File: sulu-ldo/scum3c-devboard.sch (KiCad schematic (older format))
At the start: 34 parts, among them J1 Conn_02x11_Odd_Even, J2 Conn_02x10_Odd_Even, J3 Conn_02x05_Odd_Even, J4 Conn_01x01_Male, U2 LP5907MFX-1.8, U3 TLV70311DBVR, U9AB1 ICM-20948

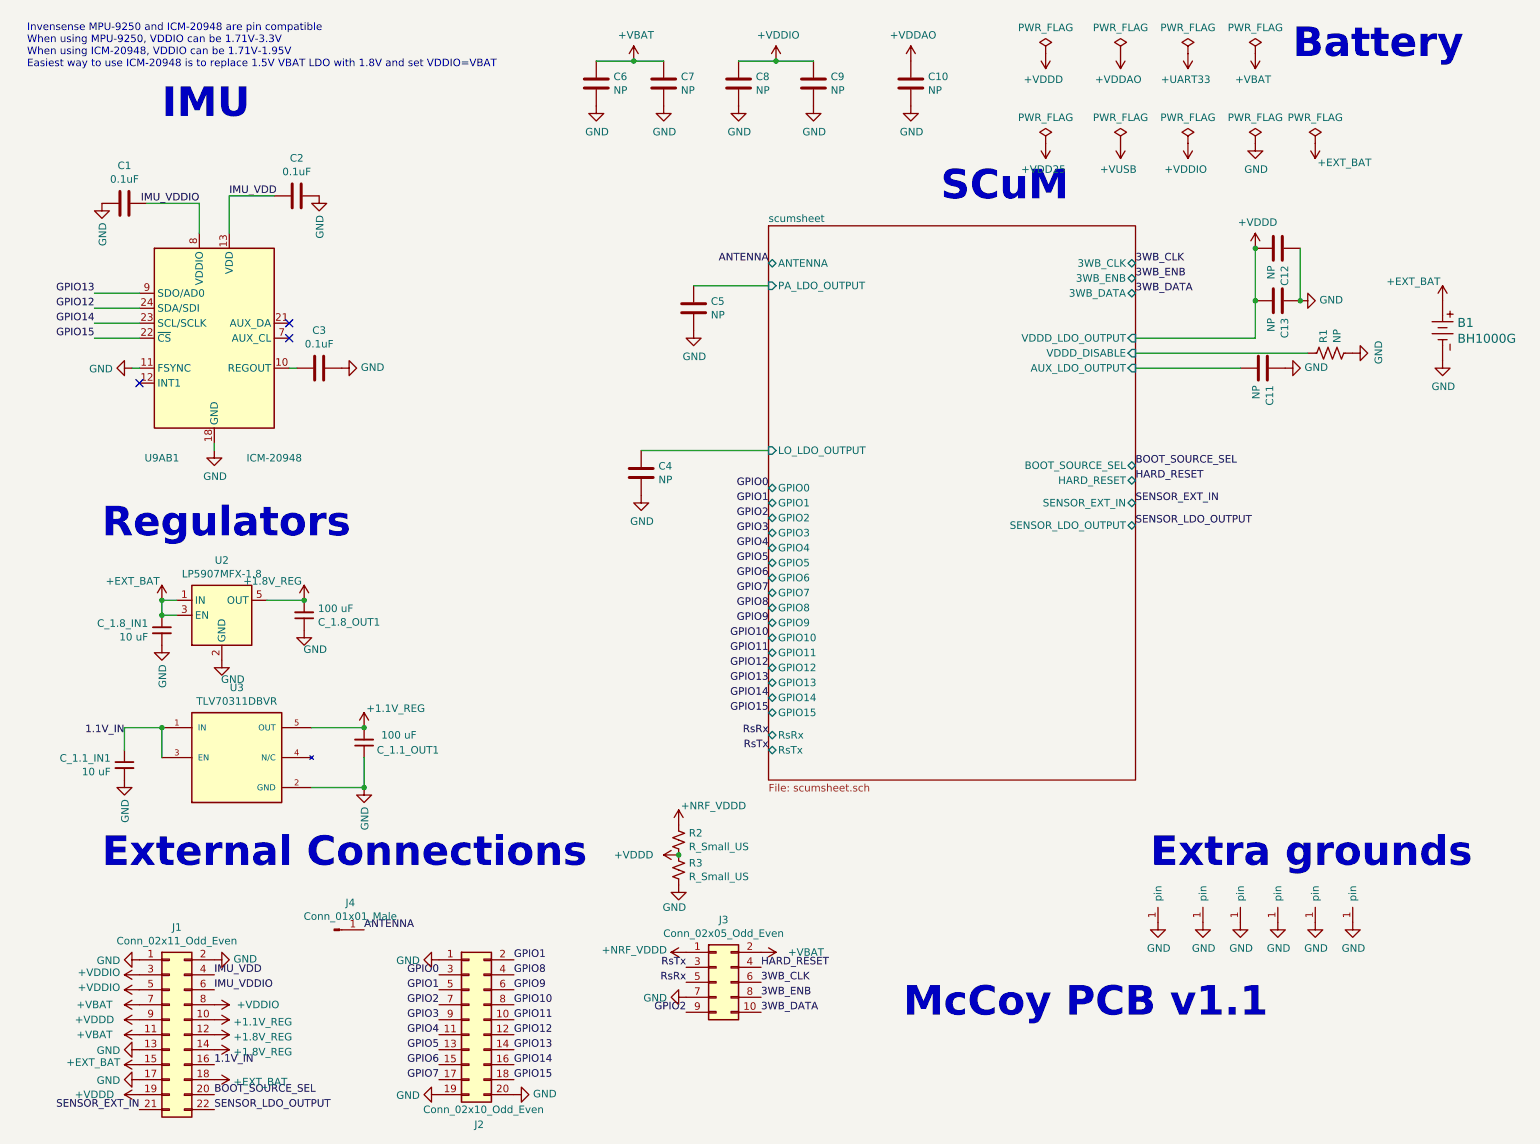
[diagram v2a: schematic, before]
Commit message: added ldos
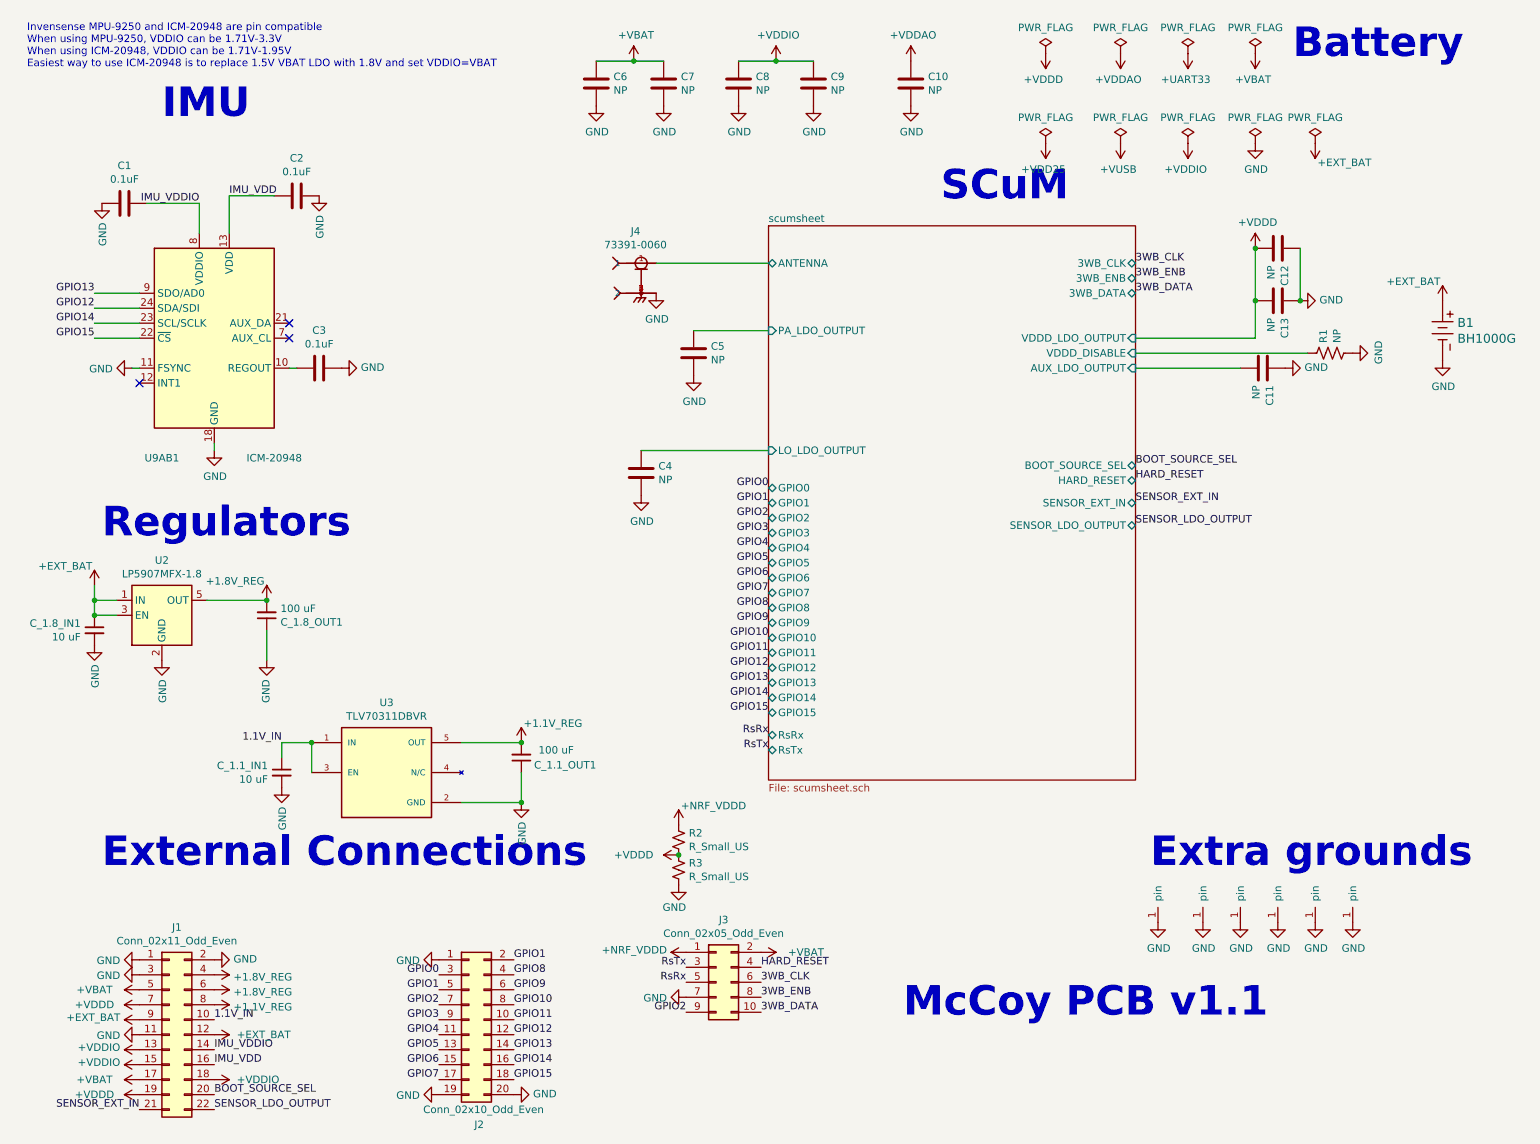
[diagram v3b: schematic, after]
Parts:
- removed J4: Conn_01x01_Male, Connector_PinHeader_2.54mm:PinHeader_1x01_P2.54mm_Vertical, symbol Connector:Conn_01x01_Male
- added J4: 73391-0060, downloaded_libs:MOLEX_73391-0060, symbol 73391-0060:73391-0060
- U3: footprint downloaded_libs:SOT95P280X145-5N -> SOT95P280X145-5N
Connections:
- net +1.1V_REG: now also J1.8 (Pin_8); no longer J1.10 (Pin_10)
- net +1.8V_REG: now also J1.4 (Pin_4), J1.6 (Pin_6); no longer J1.12 (Pin_12), J1.14 (Pin_14)
- net +EXT_BAT: now also J1.12 (Pin_12), J1.9 (Pin_9); no longer J1.15 (Pin_15), J1.18 (Pin_18)
- net +VBAT: now also J1.17 (Pin_17), J1.5 (Pin_5); no longer J1.11 (Pin_11), J1.7 (Pin_7)
- net +VDDD: now also J1.7 (Pin_7); no longer J1.9 (Pin_9)
- net +VDDIO: now also J1.13 (Pin_13), J1.15 (Pin_15), J1.18 (Pin_18); no longer J1.3 (Pin_3), J1.5 (Pin_5), J1.8 (Pin_8)
- net 1.1V_IN: now also J1.10 (Pin_10); no longer J1.16 (Pin_16)
- net GND: now also J1.11 (Pin_11), J1.3 (Pin_3), J4.2, J4.3 (2), J4.4 (2), J4.5 (2); no longer J1.13 (Pin_13), J1.17 (Pin_17)
- net IMU_VDD: now also J1.16 (Pin_16); no longer J1.4 (Pin_4)
- net IMU_VDDIO: now also J1.14 (Pin_14); no longer J1.6 (Pin_6)
- new net scumsheet/ANTENNA: J4.1
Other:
- moved on the sheet: C5, C_1.1_IN1, C_1.1_OUT1, C_1.8_IN1, C_1.8_OUT1

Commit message: put ldos on pcb
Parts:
- U3: footprint SOT95P280X145-5N -> downloaded_libs:SOT95P280X145-5N
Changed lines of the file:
@@
 F 0 "U3" H 2950 6017 50  0000 C CNN
 F 1 "TLV70311DBVR" H 2950 5926 50  0000 C CNN
-F 2 "SOT95P280X145-5N" H 2950 5550 50  0001 L BNN
+F 2 "downloaded_libs:SOT95P280X145-5N" H 2950 5550 50  0001 L BNN
 F 3 "" H 2950 5550 50  0001 L BNN
 F 4 "1.45mm" H 2950 5550 50  0001 L BNN "MAXIMUM_PACKAGE_HEIGHT"
